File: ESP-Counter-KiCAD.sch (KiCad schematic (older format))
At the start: 42 parts, among them J1 Digital_IP, J2 Motor_Ctrl, J3 LED_Indicator, J5 24V_Input, K2 G2RL-1-DC24, K5 G2RL-1-DC24, U1 ESP_12E_J1, U10 VO615A, U2 ESP_12E_J2, U3 VO615A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

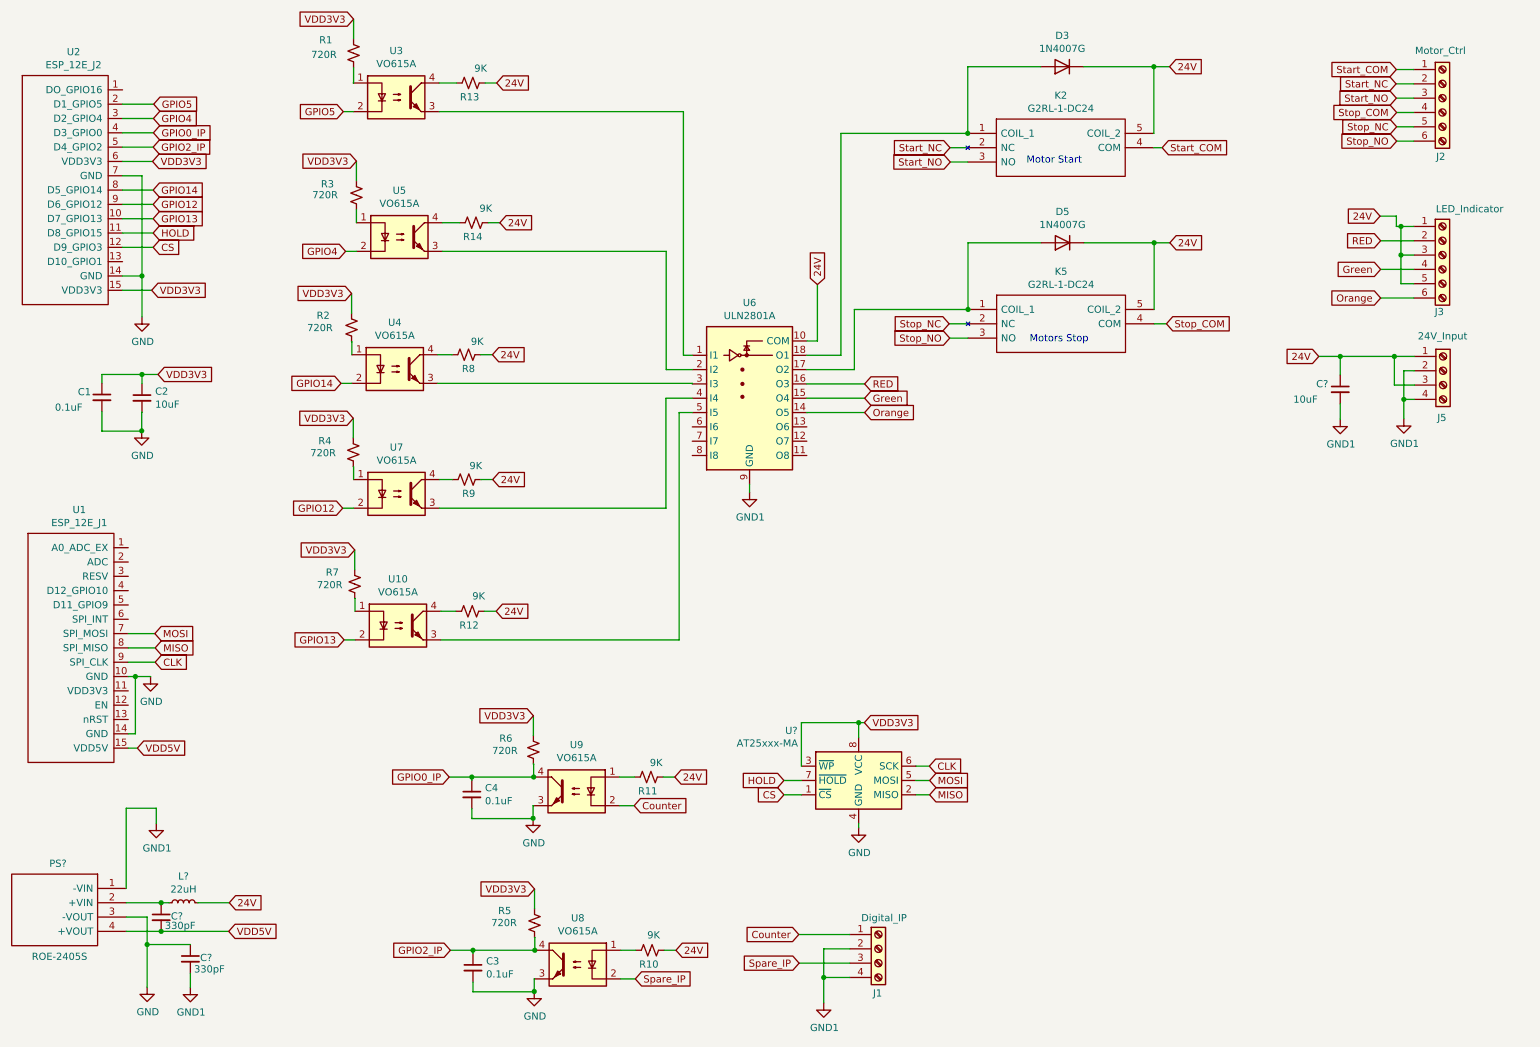
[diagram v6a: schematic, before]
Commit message: Foot print for inductor added
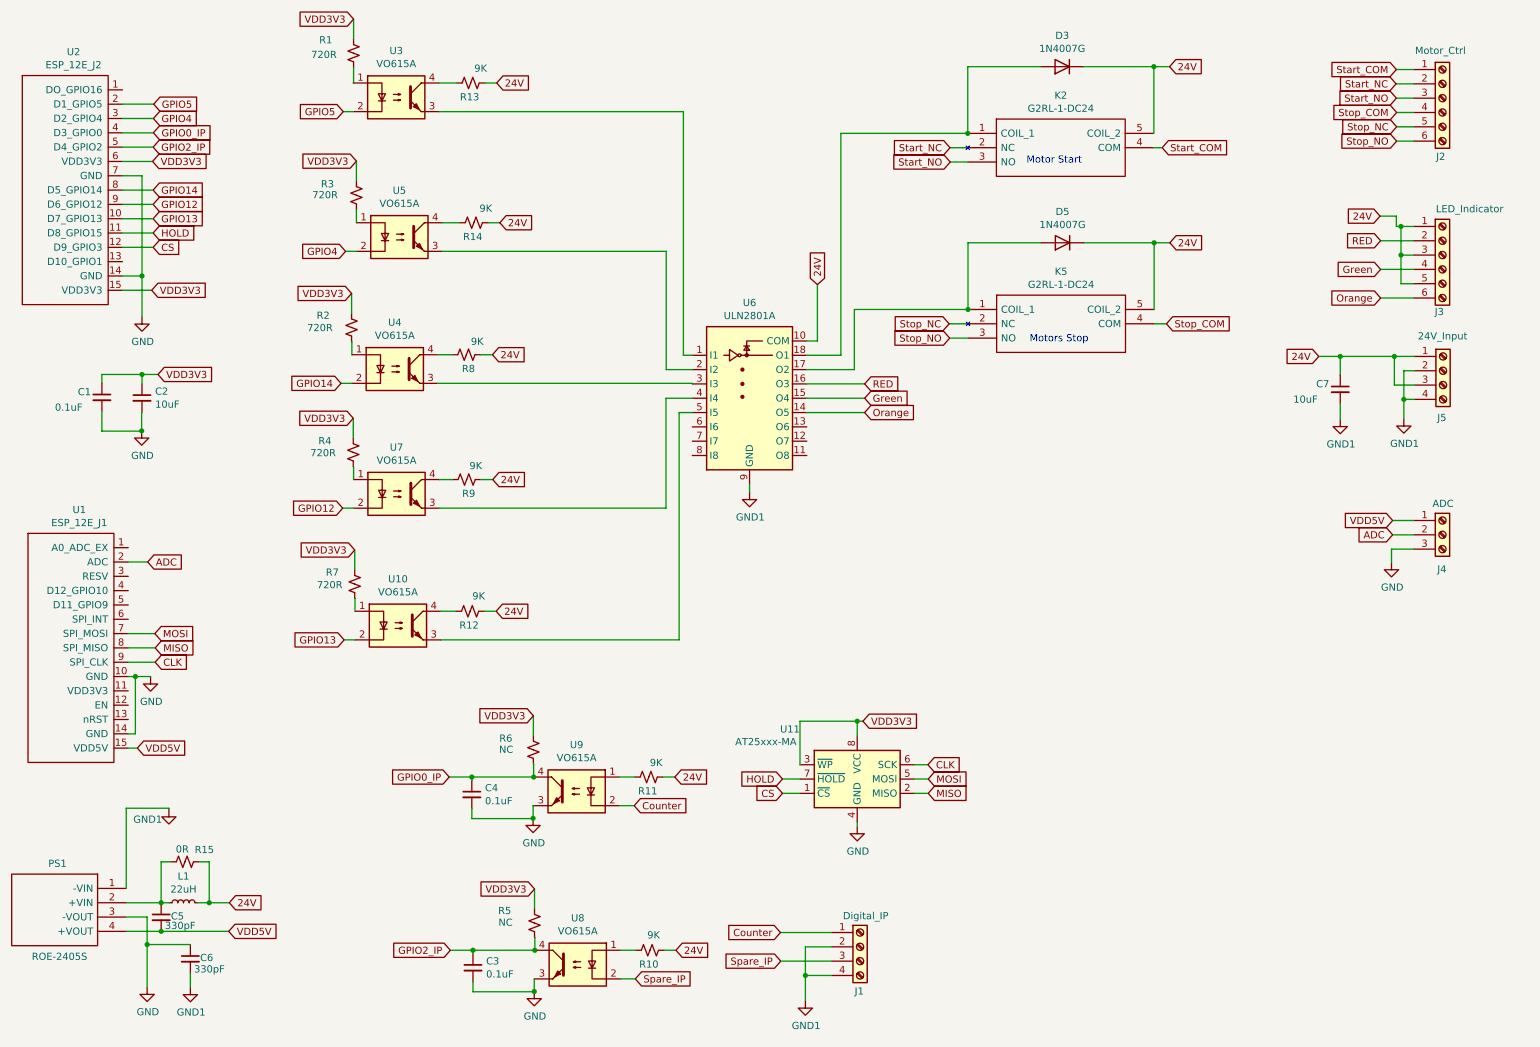
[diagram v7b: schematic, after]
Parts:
- added J4: ADC, Connector_PinHeader_2.54mm:PinHeader_1x03_P2.54mm_Vertical, symbol Connector:Screw_Terminal_01x03
- added R15: 0R, Resistor_SMD:R_0805_2012Metric_Pad1.20x1.40mm_HandSolder, symbol Device:R_Small_US
- J1, J5: footprint Connector_Phoenix_MC_HighVoltage:PhoenixContact_MCV_1,5_4-G-5.08_1x04_P5.08mm_Vertical -> Connector_PinHeader_2.54mm:PinHeader_1x04_P2.54mm_Vertical
- J2: footprint Connector_Phoenix_MC_HighVoltage:PhoenixContact_MCV_1,5_6-G-5.08_1x06_P5.08mm_Vertical -> Connector_PinHeader_2.54mm:PinHeader_1x06_P2.54mm_Vertical
- J3: footprint Connector_Phoenix_MC_HighVoltage:PhoenixContact_MCV_1,5_4-G-5.08_1x04_P5.08mm_Vertical -> Connector_PinHeader_2.54mm:PinHeader_1x06_P2.54mm_Vertical
- L1: renamed from L?; footprint (none) -> RLS-226:RLS226
- PS1: renamed from PS?; footprint ROE1205S -> ROE2450S:ROE1205S
- R5, R6: value 720R -> NC
- gave numbers to parts that had none: 4
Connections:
- net labels added: ADC
- wire segments 192 -> 202
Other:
- moved on the sheet: J1

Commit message: First iteration of routing done
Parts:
- C1, C2, C3, C4, C5, C6, C7: footprint Capacitor_SMD:C_0603_1608Metric_Pad1.08x0.95mm_HandSolder -> Capacitor_THT:C_Disc_D4.3mm_W1.9mm_P5.00mm
- R1, R10, R11, R12, R13, R14, R15, R2, R3, R4, R5, R6, R7, R8, R9: footprint Resistor_SMD:R_0805_2012Metric_Pad1.20x1.40mm_HandSolder -> Resistor_THT:R_Axial_DIN0309_L9.0mm_D3.2mm_P15.24mm_Horizontal
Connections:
- wire segments 202 -> 204
- no-connect marks 0 -> 17
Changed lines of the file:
@@
 F 0 "R1" H 2834 986 50  0000 L CNN
 F 1 "720R" H 2778 884 50  0000 L CNN
-F 2 "Resistor_SMD:R_0805_2012Metric_Pad1.20x1.40mm_HandSolder" H 3074 894 50  0001 C CNN
+F 2 "Resistor_THT:R_Axial_DIN0309_L9.0mm_D3.2mm_P15.24mm_Horizontal" H 3074 894 50  0001 C CNN
 F 3 "~" H 3074 894 50  0001 C CNN
 	1    3074 894
@@
 F 0 "R3" H 2846 1964 50  0000 L CNN
 F 1 "720R" H 2786 1888 50  0000 L CNN
-F 2 "Resistor_SMD:R_0805_2012Metric_Pad1.20x1.40mm_HandSolder" H 3094 1886 50  0001 C CNN
+F 2 "Resistor_THT:R_Axial_DIN0309_L9.0mm_D3.2mm_P15.24mm_Horizontal" H 3094 1886 50  0001 C CNN
 F 3 "~" H 3094 1886 50  0001 C CNN
 	1    3094 1886
@@
 F 0 "R2" H 2816 2894 50  0000 L CNN
 F 1 "720R" H 2750 2808 50  0000 L CNN
-F 2 "Resistor_SMD:R_0805_2012Metric_Pad1.20x1.40mm_HandSolder" H 3060 2810 50  0001 C CNN
+F 2 "Resistor_THT:R_Axial_DIN0309_L9.0mm_D3.2mm_P15.24mm_Horizontal" H 3060 2810 50  0001 C CNN
 F 3 "~" H 3060 2810 50  0001 C CNN
 	1    3060 2810
@@
 F 0 "R4" H 2828 3762 50  0000 L CNN
 F 1 "720R" H 2772 3678 50  0000 L CNN
-F 2 "Resistor_SMD:R_0805_2012Metric_Pad1.20x1.40mm_HandSolder" H 3072 3682 50  0001 C CNN
+F 2 "Resistor_THT:R_Axial_DIN0309_L9.0mm_D3.2mm_P15.24mm_Horizontal" H 3072 3682 50  0001 C CNN
 F 3 "~" H 3072 3682 50  0001 C CNN
 	1    3072 3682
@@
 F 0 "R7" H 2880 4684 50  0000 L CNN
 F 1 "720R" H 2818 4596 50  0000 L CNN
-F 2 "Resistor_SMD:R_0805_2012Metric_Pad1.20x1.40mm_HandSolder" H 3082 4602 50  0001 C CNN
+F 2 "Resistor_THT:R_Axial_DIN0309_L9.0mm_D3.2mm_P15.24mm_Horizontal" H 3082 4602 50  0001 C CNN
 F 3 "~" H 3082 4602 50  0001 C CNN
 	1    3082 4602
@@
 F 0 "R13" V 3794 1042 50  0000 L CNN
 F 1 "9K" V 3994 988 50  0000 L CNN
-F 2 "Resistor_SMD:R_0805_2012Metric_Pad1.20x1.40mm_HandSolder" H 3892 1102 50  0001 C CNN
+F 2 "Resistor_THT:R_Axial_DIN0309_L9.0mm_D3.2mm_P15.24mm_Horizontal" H 3892 1102 50  0001 C CNN
 F 3 "~" H 3892 1102 50  0001 C CNN
 	1    3892 1102
@@
 F 0 "R14" V 3816 2018 50  0000 L CNN
 F 1 "9K" V 4014 1950 50  0000 L CNN
-F 2 "Resistor_SMD:R_0805_2012Metric_Pad1.20x1.40mm_HandSolder" H 3914 2078 50  0001 C CNN
+F 2 "Resistor_THT:R_Axial_DIN0309_L9.0mm_D3.2mm_P15.24mm_Horizontal" H 3914 2078 50  0001 C CNN
 F 3 "~" H 3914 2078 50  0001 C CNN
 	1    3914 2078
@@
 F 0 "R8" V 3764 2940 50  0000 L CNN
 F 1 "9K" V 3954 2880 50  0000 L CNN
-F 2 "Resistor_SMD:R_0805_2012Metric_Pad1.20x1.40mm_HandSolder" H 3862 3000 50  0001 C CNN
+F 2 "Resistor_THT:R_Axial_DIN0309_L9.0mm_D3.2mm_P15.24mm_Horizontal" H 3862 3000 50  0001 C CNN
 F 3 "~" H 3862 3000 50  0001 C CNN
 	1    3862 3000
@@
 F 0 "R9" V 3766 3812 50  0000 L CNN
 F 1 "9K" V 3960 3764 50  0000 L CNN
-F 2 "Resistor_SMD:R_0805_2012Metric_Pad1.20x1.40mm_HandSolder" H 3864 3872 50  0001 C CNN
+F 2 "Resistor_THT:R_Axial_DIN0309_L9.0mm_D3.2mm_P15.24mm_Horizontal" H 3864 3872 50  0001 C CNN
 F 3 "~" H 3864 3872 50  0001 C CNN
 	1    3864 3872
@@
 F 0 "R12" V 3790 4732 50  0000 L CNN
 F 1 "9K" V 3994 4688 50  0000 L CNN
-F 2 "Resistor_SMD:R_0805_2012Metric_Pad1.20x1.40mm_HandSolder" H 3888 4792 50  0001 C CNN
+F 2 "Resistor_THT:R_Axial_DIN0309_L9.0mm_D3.2mm_P15.24mm_Horizontal" H 3888 4792 50  0001 C CNN
 F 3 "~" H 3888 4792 50  0001 C CNN
 	1    3888 4792
@@
 	1    0    0    -1
 $EndComp
-Wire Wire Line
-	5840 3904 5840 3962
 Text GLabel 8774 988  2    50   Input ~ 0
 24V
@@
 F 0 "C2" H 1688 3348 50  0000 L CNN
 F 1 "10uF" H 1688 3257 50  0000 L CNN
-F 2 "Capacitor_SMD:C_0603_1608Metric_Pad1.08x0.95mm_HandSolder" H 1596 3302 50  0001 C CNN
+F 2 "Capacitor_THT:C_Disc_D4.3mm_W1.9mm_P5.00mm" H 1596 3302 50  0001 C CNN
 F 3 "~" H 1596 3302 50  0001 C CNN
 	1    1596 3302
@@
 F 0 "C1" H 1148 3336 50  0000 L CNN
 F 1 "0.1uF" H 988 3228 50  0000 L CNN
-F 2 "Capacitor_SMD:C_0603_1608Metric_Pad1.08x0.95mm_HandSolder" H 1316 3298 50  0001 C CNN
+F 2 "Capacitor_THT:C_Disc_D4.3mm_W1.9mm_P5.00mm" H 1316 3298 50  0001 C CNN
 F 3 "~" H 1316 3298 50  0001 C CNN
 	1    1316 3298
@@
 F 0 "R11" V 5038 5890 50  0000 L CNN
 F 1 "9K" V 5236 5854 50  0000 L CNN
-F 2 "Resistor_SMD:R_0805_2012Metric_Pad1.20x1.40mm_HandSolder" H 5136 5950 50  0001 C CNN
+F 2 "Resistor_THT:R_Axial_DIN0309_L9.0mm_D3.2mm_P15.24mm_Horizontal" H 5136 5950 50  0001 C CNN
 F 3 "~" H 5136 5950 50  0001 C CNN
 	1    5136 5950
@@
 F 0 "R6" H 4092 5840 50  0000 L CNN
 F 1 "NC" H 4090 5762 50  0000 L CNN
-F 2 "Resistor_SMD:R_0805_2012Metric_Pad1.20x1.40mm_HandSolder" H 4330 5760 50  0001 C CNN
+F 2 "Resistor_THT:R_Axial_DIN0309_L9.0mm_D3.2mm_P15.24mm_Horizontal" H 4330 5760 50  0001 C CNN
 F 3 "~" H 4330 5760 50  0001 C CNN
 	1    4330 5760
@@
 F 0 "C4" H 3992 6118 50  0000 L CNN
 F 1 "0.1uF" H 3992 6027 50  0000 L CNN
-F 2 "Capacitor_SMD:C_0603_1608Metric_Pad1.08x0.95mm_HandSolder" H 3900 6072 50  0001 C CNN
+F 2 "Capacitor_THT:C_Disc_D4.3mm_W1.9mm_P5.00mm" H 3900 6072 50  0001 C CNN
 F 3 "~" H 3900 6072 50  0001 C CNN
 	1    3900 6072
@@
 F 0 "R10" V 5046 7100 50  0000 L CNN
 F 1 "9K" V 5250 7090 50  0000 L CNN
-F 2 "Resistor_SMD:R_0805_2012Metric_Pad1.20x1.40mm_HandSolder" H 5144 7160 50  0001 C CNN
+F 2 "Resistor_THT:R_Axial_DIN0309_L9.0mm_D3.2mm_P15.24mm_Horizontal" H 5144 7160 50  0001 C CNN
 F 3 "~" H 5144 7160 50  0001 C CNN
 	1    5144 7160
@@
 F 0 "R5" H 4084 7056 50  0000 L CNN
 F 1 "NC" H 4086 6974 50  0000 L CNN
-F 2 "Resistor_SMD:R_0805_2012Metric_Pad1.20x1.40mm_HandSolder" H 4338 6970 50  0001 C CNN
+F 2 "Resistor_THT:R_Axial_DIN0309_L9.0mm_D3.2mm_P15.24mm_Horizontal" H 4338 6970 50  0001 C CNN
 F 3 "~" H 4338 6970 50  0001 C CNN
 	1    4338 6970
@@
 F 0 "C3" H 4000 7328 50  0000 L CNN
 F 1 "0.1uF" H 4000 7237 50  0000 L CNN
-F 2 "Capacitor_SMD:C_0603_1608Metric_Pad1.08x0.95mm_HandSolder" H 3908 7282 50  0001 C CNN
+F 2 "Capacitor_THT:C_Disc_D4.3mm_W1.9mm_P5.00mm" H 3908 7282 50  0001 C CNN
 F 3 "~" H 3908 7282 50  0001 C CNN
 	1    3908 7282
@@
 	10390 2304 10390 2504
 Wire Wire Line
-	9816 3012 9966 3012
+	9816 3012 9878 3012
 Wire Wire Line
 	10344 3012 10344 3014
@@
 F 0 "C7" H 9798 3280 50  0000 L CNN
 F 1 "10uF" H 9638 3172 50  0000 L CNN
-F 2 "Capacitor_SMD:C_0603_1608Metric_Pad1.08x0.95mm_HandSolder" H 9966 3242 50  0001 C CNN
+F 2 "Capacitor_THT:C_Disc_D4.3mm_W1.9mm_P5.00mm" H 9966 3242 50  0001 C CNN
 F 3 "~" H 9966 3242 50  0001 C CNN
 	1    9966 3242
@@
 Text GLabel 2202 7028 2    50   Input ~ 0
 VDD5V
-Wire Wire Line
-	1486 7028 1730 7028
 $Comp
 L power:GND #PWR0103
@@
 	1486 6728 1486 6168
 Wire Wire Line
-	1730 7032 1730 7028
-Connection ~ 1730 7028
-Wire Wire Line
-	1730 7028 2202 7028
-Wire Wire Line
 	1730 6828 1730 6830
 Connection ~ 1730 6828
@@
 F 0 "C5" H 1798 6938 50  0000 L CNN
 F 1 "330pF" H 1756 6872 50  0000 L CNN
-F 2 "Capacitor_SMD:C_0603_1608Metric_Pad1.08x0.95mm_HandSolder" H 1730 6930 50  0001 C CNN
+F 2 "Capacitor_THT:C_Disc_D4.3mm_W1.9mm_P5.00mm" H 1730 6930 50  0001 C CNN
 F 3 "~" H 1730 6930 50  0001 C CNN
 	1    1730 6930
@@
 F 0 "C6" H 2002 7228 50  0000 L CNN
 F 1 "330pF" H 1960 7148 50  0000 L CNN
-F 2 "Capacitor_SMD:C_0603_1608Metric_Pad1.08x0.95mm_HandSolder" H 1934 7220 50  0001 C CNN
+F 2 "Capacitor_THT:C_Disc_D4.3mm_W1.9mm_P5.00mm" H 1934 7220 50  0001 C CNN
 F 3 "~" H 1934 7220 50  0001 C CNN
 	1    1934 7220
@@
 Wire Wire Line
 	6070 6064 6192 6064
-Wire Wire Line
-	1500 5648 1550 5648
-Wire Wire Line
-	1550 5648 1550 5248
-Wire Wire Line
-	1500 5248 1550 5248
-Connection ~ 1550 5248
-Wire Wire Line
-	1550 5248 1656 5248
 Text GLabel 1636 4448 2    50   Input ~ 0
 ADC
@@
 F 0 "R15" V 1812 6610 50  0000 L CNN
 F 1 "0R" V 1808 6478 50  0000 L CNN
-F 2 "Resistor_SMD:R_0805_2012Metric_Pad1.20x1.40mm_HandSolder" H 1896 6542 50  0001 C CNN
+F 2 "Resistor_THT:R_Axial_DIN0309_L9.0mm_D3.2mm_P15.24mm_Horizontal" H 1896 6542 50  0001 C CNN
 F 3 "~" H 1896 6542 50  0001 C CNN
 	1    1896 6542
@@
 Wire Wire Line
 	1486 6168 1784 6168
+Wire Wire Line
+	1486 7028 1700 7028
+Wire Wire Line
+	1700 7028 1700 7030
+Wire Wire Line
+	1700 7030 1730 7030
+Wire Wire Line
+	1730 7030 2202 7030
+Wire Wire Line
+	2202 7030 2202 7028
+Connection ~ 1730 7030
+NoConn ~ 1460 1150
+NoConn ~ 1460 2350
+NoConn ~ 1500 4348
+NoConn ~ 1500 4548
+NoConn ~ 1500 4648
+NoConn ~ 1500 4748
+NoConn ~ 1500 4848
+NoConn ~ 1500 5348
+NoConn ~ 1500 5448
+NoConn ~ 1500 5548
+NoConn ~ 5440 3504
+NoConn ~ 5440 3604
+NoConn ~ 5440 3704
+NoConn ~ 6240 3504
+NoConn ~ 6240 3604
+NoConn ~ 6240 3704
+$Comp
+L power:PWR_FLAG #FLG0101
+U 1 1 6027A2E2
+P 9878 3012
+F 0 "#FLG0101" H 9878 3087 50  0001 C CNN
+F 1 "PWR_FLAG" H 9878 3185 50  0000 C CNN
+F 2 "" H 9878 3012 50  0001 C CNN
+F 3 "~" H 9878 3012 50  0001 C CNN
+	1    9878 3012
+	1    0    0    -1
+$EndComp
+Connection ~ 9878 3012
+Wire Wire Line
+	9878 3012 9966 3012
+$Comp
+L power:PWR_FLAG #FLG0102
+U 1 1 6027C72E
+P 6106 3940
+F 0 "#FLG0102" H 6106 4015 50  0001 C CNN
+F 1 "PWR_FLAG" V 6106 4068 50  0000 L CNN
+F 2 "" H 6106 3940 50  0001 C CNN
+F 3 "~" H 6106 3940 50  0001 C CNN
+	1    6106 3940
+	0    1    1    0
+$EndComp
+Wire Wire Line
+	5840 3904 5840 3940
+Wire Wire Line
+	6106 3940 5840 3940
+Connection ~ 5840 3940
+Wire Wire Line
+	5840 3940 5840 3962
+Wire Wire Line
+	1500 5248 1656 5248
+NoConn ~ 1500 5648
 $EndSCHEMATC
